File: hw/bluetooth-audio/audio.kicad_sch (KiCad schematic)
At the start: 39 parts, among them J1 AudioJack4_Ground, U4 ES8388

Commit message: Schematic: split supply into separate audio and system 3V3 rails
First design work since the April 2025 production release. Sixteen months of
edits had accumulated uncommitted; this captures the schematic and board state.

Power topology change: the single 3.3 V supply is now two independent rails,
+3V3_SYS and +3V3_AUDIO, each with its own regulator (U7, U8) and test point
(TEST_3V3_SYS, TEST_3V3_AUDIO). This isolates the ES8388 and the mic from the
~250 mA Bluetooth TX bursts on the ESP32 rail, which design-review-v1 flagged
as an S2 defect and the ES8388 user guide asks for directly.

Also addresses the S1 defects from the review (owner-applied): ES8388 CE pin
pulled down to DGND so the I2C address is determined rather than floating, and
the ESP32 CAP1 10 nF cap fitted.

Both rails are currently NCP1117-3.3 in SOT-223. The topology is right but the
parts are not yet the ones specified in docs/requirements-design.md: Rail A
should become AP7361C-33Y5 (SOT-89-5, ultra-low dropout, needed so the rail
survives on battery) and Rail B an LP5907MFX-3.3 (6.5 uVRMS, the point of
having a separate analog rail at all). Two SOT-223 parts also spend board area
the review specifically asked to reclaim.

Co-Authored-By: Claude Opus 5 <noreply@anthropic.com>
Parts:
- added C46: 100nF, Capacitor_SMD:C_0402_1005Metric, symbol Device:C_Small
- added R16: 10R, Resistor_SMD:R_0402_1005Metric, symbol Device:R_Small
- added R27: 10k, Resistor_SMD:R_0402_1005Metric, symbol Device:R_Small
- added U3: TS5A23159DGS, Package_SO:TSSOP-10_3x3mm_P0.5mm, symbol Analog_Switch:TS5A23159DGS
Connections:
- net GND: now also C46.2, R27.2, U3.3 (GND)
- net I2C_AD: no longer U4.26 (CE)
- net LIN2: now also U3.2
- net LOUT1: now also U4.12 (LOUT1), U3.9; no longer J1.T, R7.2
- net RIN2: now also U3.4
- net ROUT1: now also U4.11 (ROUT1), U3.7; no longer J1.R1, R8.2
- net at C25.2: now also U3.6; no longer U4.11 (ROUT1)
- net at C23.2: now also U3.10; no longer U4.12 (LOUT1)
- net +1V8 renamed +3V3_AUDIO
- net +3V3_AUDIO: now also R16.1
- net +3V3 renamed AVDD
- net AVDD: now also C46.1, R16.2, U3.8 (VCC)
- new net: J1.R1, R7.2
- new net: J1.T, R8.2
- new net: R27.1, U4.26 (CE)
- new net AUDIO_IN_EN: U3.5
- new net AUDIO_OUT_EN: U3.1
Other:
- note added: "Separation between digital and audio VCC TODO confirm from Datasheet"
- note added: "TODO replace with 3 pole"
- note removed: "Check connections on audio jack"
- moved on the sheet: J1, TP6

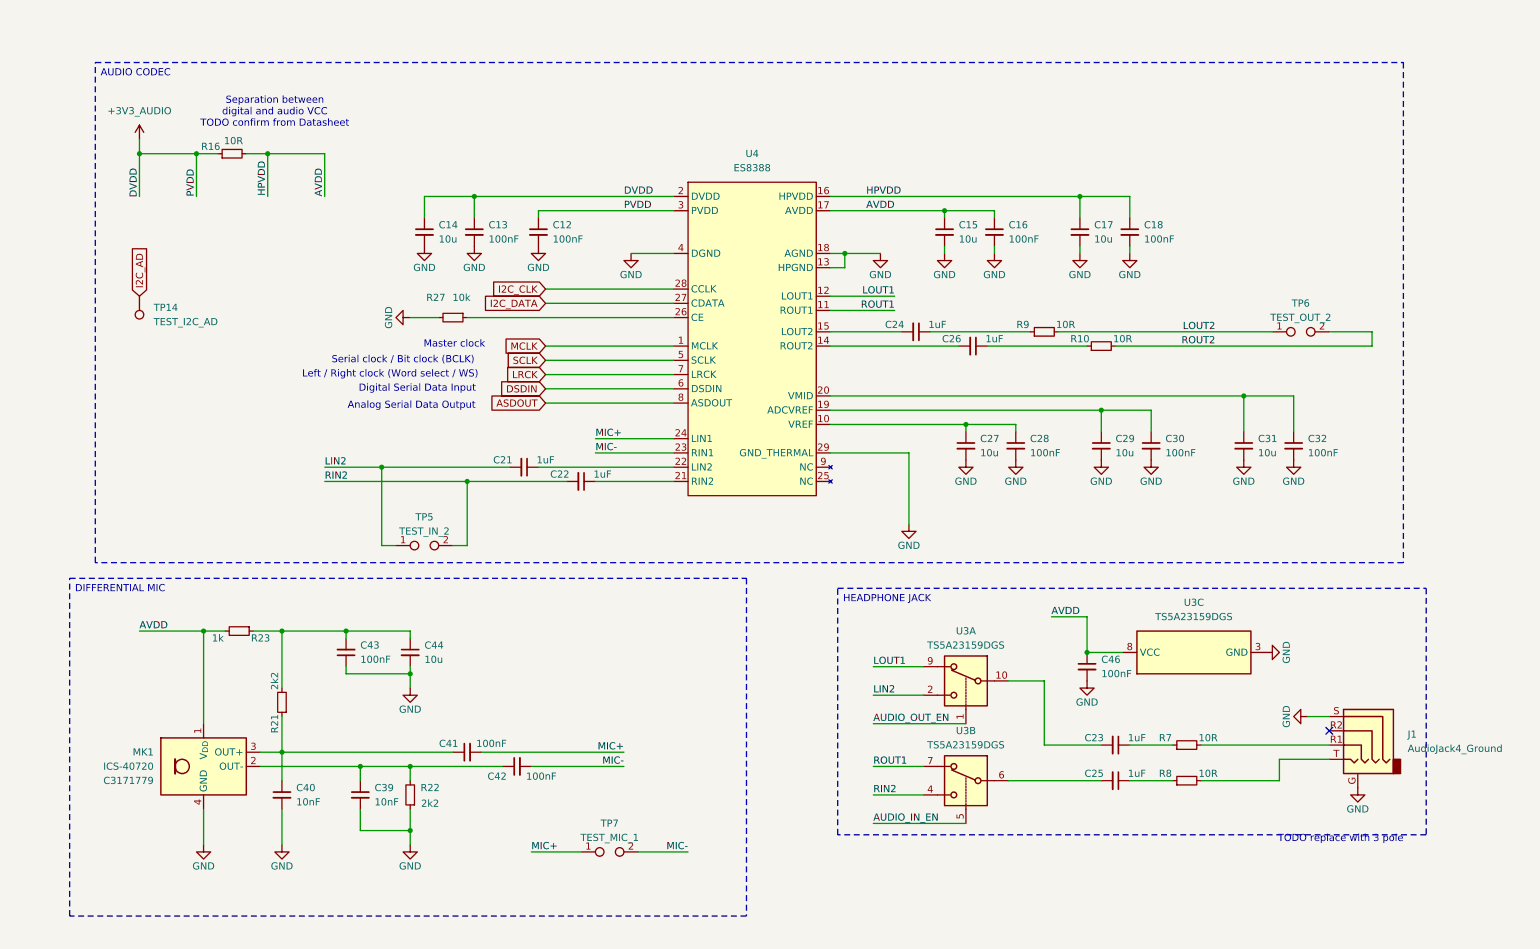
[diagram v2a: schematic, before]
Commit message: Rev B micro sheet: correctness fixes, CH340 load switch, full ESP32 GPIO map
Micro-sheet fixes (netlist-verified):
- UART TX/RX crossover corrected (U0RXD<->CH340 TXD, U0TXD<->CH340 RXD)
- Flash IO2/IO3 uncrossed (GPIO9/SPIWP->IO2, GPIO10/SPIHD->IO3)
- Digital rail unified to +3V3_SYS; EN pull-up (R11) reconnected

CH340K high-side load switch (delta #16):
- Q2 AO3401A (SOT-23, LCSC C15127) + R40 100k gate pull-down = default-ON
  so the ROM bootloader is powered for USB flashing; gate CH340_EN on GPIO21,
  firmware drives high to disable the bridge on battery

Full ESP32 interface wired (see design-overview.md 3.8):
- EN1->16, EN2->17, AUDIO_VCC_EN->4, AUDIO_SW->5, CH340_EN->21, CHARGE_EN->2
- /PGOOD->38, /CHG->32; ADC1 senses BAT_ADC->34, USB_CC1->36, USB_CC2->37,
  USB_VBUS_SENSE->39; GPIO33 spare
- AUDIO_SW drives both TS5A23159 inputs (LOW=RX, HIGH=TX); pinout verified
  against TI datasheet (COM=jack, NC=codec-out, NO=codec-in, both channels)

Docs:
- design-overview.md: committed GPIO map with strapping-pin FW/HW implications
  (3.8), AUDIO_SW/CHARGE_EN firmware notes (9), updated status (10)
- design-review-micro.md: micro-sheet systems review
- added WCH CH340 datasheet; updated TODO
- gitignore MCP snapshot/log artifacts

Co-Authored-By: Claude Opus 4.8 <noreply@anthropic.com>
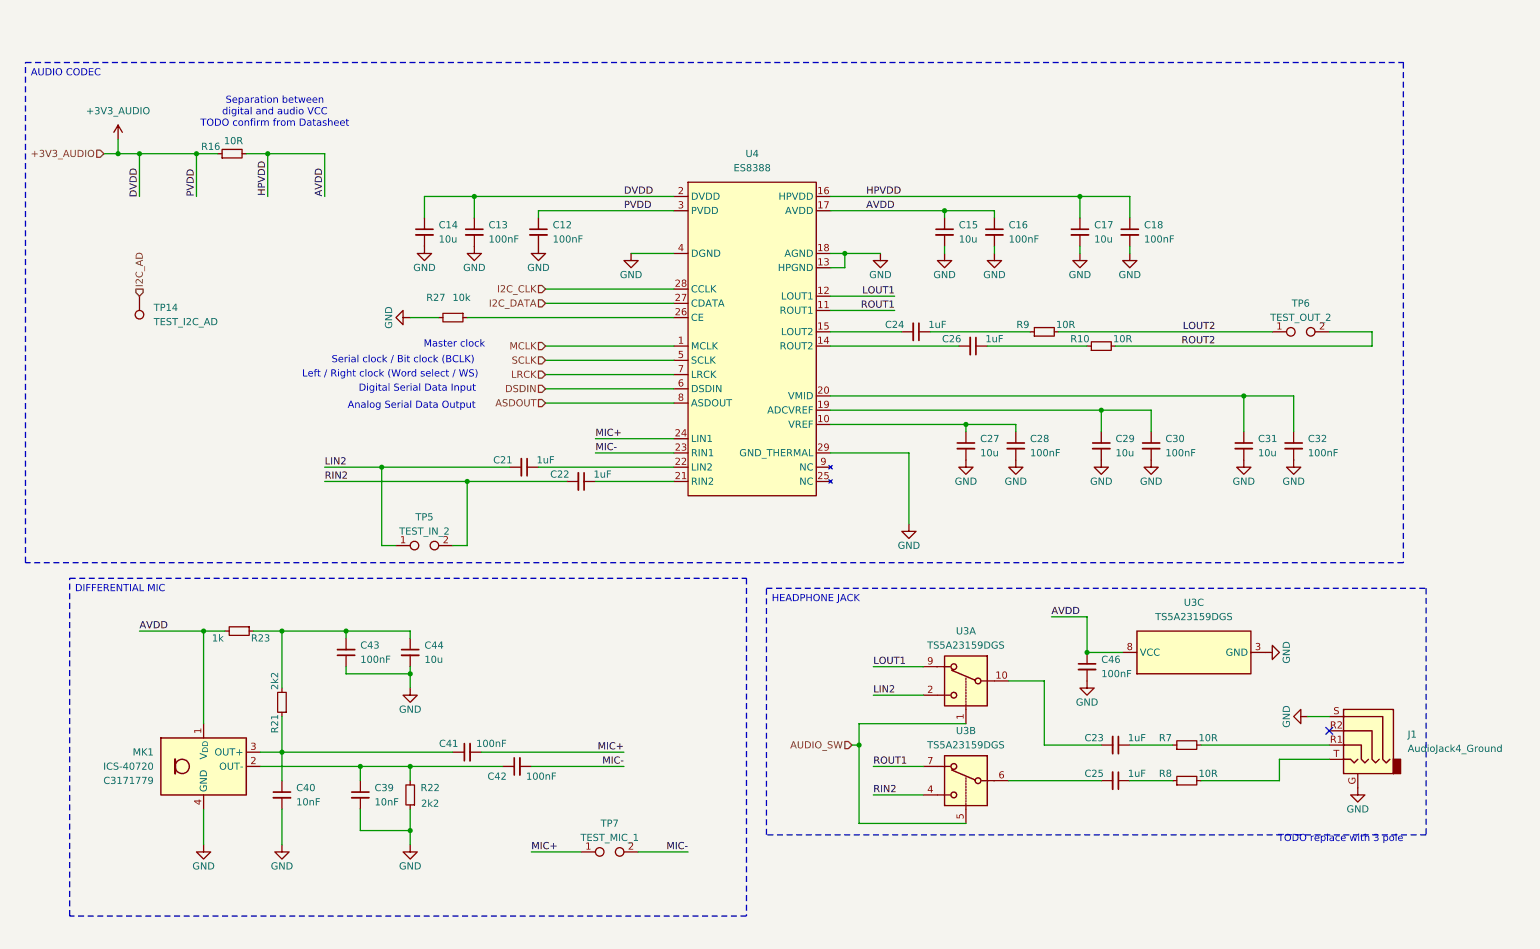
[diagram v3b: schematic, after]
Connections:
- net AUDIO_OUT_EN is gone; now on net AUDIO_SW: U3.1
- net AUDIO_IN_EN renamed AUDIO_SW
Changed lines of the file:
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@@
 	(text_box "HEADPHONE JACK\n"
 		(exclude_from_sim no)
-		(at 165.1 119.38 0)
-		(size 104.902 43.942)
+		(at 152.4 119.38 0)
+		(size 117.602 43.942)
 		(margins 0.9525 0.9525 0.9525 0.9525)
 		(stroke
@@
 	(text_box "AUDIO CODEC\n"
 		(exclude_from_sim no)
-		(at 32.766 25.654 0)
-		(size 233.172 89.154)
+		(at 20.32 25.654 0)
+		(size 245.618 89.154)
 		(margins 0.9525 0.9525 0.9525 0.9525)
 		(stroke
@@
 	)
 	(junction
+		(at 36.83 41.91)
+		(diameter 0)
+		(color 0 0 0 0)
+	)
+	(junction
 		(at 52.07 127)
 		(diameter 0)
@@
 	)
 	(junction
+		(at 168.91 147.32)
+		(diameter 0)
+		(color 0 0 0 0)
+	)
+	(junction
 		(at 88.9 151.13)
 		(diameter 0)
@@
 	(wire
 		(pts
+			(xy 168.91 161.29) (xy 187.96 161.29)
+		)
+		(stroke
+			(width 0)
+			(type default)
+		)
+	)
+	(wire
+		(pts
 			(xy 121.92 100.33) (xy 135.89 100.33)
 		)
@@
 	(wire
 		(pts
+			(xy 34.29 41.91) (xy 36.83 41.91)
+		)
+		(stroke
+			(width 0)
+			(type default)
+		)
+	)
+	(wire
+		(pts
 			(xy 63.5 41.91) (xy 63.5 49.53)
 		)
@@
 	(wire
 		(pts
-			(xy 171.45 143.51) (xy 187.96 143.51)
+			(xy 163.83 67.31) (xy 175.26 67.31)
 		)
 		(stroke
@@
 	(wire
 		(pts
-			(xy 163.83 67.31) (xy 175.26 67.31)
+			(xy 171.45 138.43) (xy 180.34 138.43)
 		)
 		(stroke
@@
 	(wire
 		(pts
-			(xy 171.45 138.43) (xy 180.34 138.43)
+			(xy 113.03 86.36) (xy 135.89 86.36)
 		)
 		(stroke
@@
 	(wire
 		(pts
-			(xy 113.03 86.36) (xy 135.89 86.36)
+			(xy 163.83 49.53) (xy 208.28 49.53)
 		)
 		(stroke
@@
 	(wire
 		(pts
-			(xy 163.83 49.53) (xy 208.28 49.53)
+			(xy 99.06 111.76) (xy 96.52 111.76)
 		)
 		(stroke
@@
 	(wire
 		(pts
-			(xy 99.06 111.76) (xy 96.52 111.76)
+			(xy 36.83 41.91) (xy 40.64 41.91)
 		)
 		(stroke
@@
 	(wire
 		(pts
+			(xy 168.91 147.32) (xy 168.91 161.29)
+		)
+		(stroke
+			(width 0)
+			(type default)
+		)
+	)
+	(wire
+		(pts
 			(xy 80.01 151.13) (xy 88.9 151.13)
 		)
@@
 	(wire
 		(pts
-			(xy 40.64 41.91) (xy 40.64 39.37)
+			(xy 36.83 41.91) (xy 36.83 39.37)
 		)
 		(stroke
@@
 	(wire
 		(pts
+			(xy 168.91 143.51) (xy 187.96 143.51)
+		)
+		(stroke
+			(width 0)
+			(type default)
+		)
+	)
+	(wire
+		(pts
 			(xy 184.15 59.69) (xy 184.15 58.42)
 		)
@@
 	(wire
 		(pts
+			(xy 167.64 147.32) (xy 168.91 147.32)
+		)
+		(stroke
+			(width 0)
+			(type default)
+		)
+	)
+	(wire
+		(pts
 			(xy 209.55 130.81) (xy 215.9 130.81)
 		)
@@
 	(wire
 		(pts
+			(xy 168.91 143.51) (xy 168.91 147.32)
+		)
+		(stroke
+			(width 0)
+			(type default)
+		)
+	)
+	(wire
+		(pts
 			(xy 214.63 76.2) (xy 260.35 76.2)
 		)
@@
 	(wire
 		(pts
-			(xy 171.45 161.29) (xy 187.96 161.29)
-		)
-		(stroke
-			(width 0)
-			(type default)
-		)
-	)
-	(wire
-		(pts
 			(xy 52.07 165.1) (xy 52.07 158.75)
 		)
@@
 		)
 	)
-	(label "AUDIO_IN_EN"
-		(at 171.45 161.29 0)
-		(effects
-			(font
-				(size 1.27 1.27)
-			)
-			(justify left bottom)
-		)
-	)
 	(label "PVDD"
 		(at 50.8 49.53 90)
@@
 		)
 	)
-	(label "AUDIO_OUT_EN"
-		(at 171.45 143.51 0)
-		(effects
-			(font
-				(size 1.27 1.27)
-			)
-			(justify left bottom)
-		)
-	)
 	(label "HPVDD"
 		(at 170.18 49.53 0)
@@
 		)
 	)
-	(global_label "LRCK"
+	(hierarchical_label "LRCK"
 		(shape input)
 		(at 113.03 81.28 180)
-		(fields_autoplaced yes)
 		(effects
 			(font
@@
 			(justify right)
 		)
-		(property "Intersheetrefs" "${INTERSHEET_REFS}"
-			(at 105.2067 81.28 0)
-			(hide yes)
-			(show_name no)
-			(do_not_autoplace no)
-			(effects
-				(font
-					(size 1.27 1.27)
-				)
-				(justify right)
+	)
+	(hierarchical_label "I2C_AD"
+		(shape input)
+		(at 40.64 67.31 90)
+		(effects
+			(font
+				(size 1.27 1.27)
 			)
+			(justify left)
 		)
 	)
-	(global_label "I2C_DATA"
+	(hierarchical_label "I2C_CLK"
 		(shape input)
-		(at 113.03 68.58 180)
-		(fields_autoplaced yes)
+		(at 113.03 66.04 180)
 		(effects
 			(font
@@
 			(justify right)
 		)
-		(property "Intersheetrefs" "${INTERSHEET_REFS}"
-			(at 101.5781 68.58 0)
-			(hide yes)
-			(show_name no)
-			(do_not_autoplace no)
-			(effects
-				(font
-					(size 1.27 1.27)
-				)
-				(justify right)
+	)
+	(hierarchical_label "+3V3_AUDIO"
+		(shape input)
+		(at 34.29 41.91 180)
+		(effects
+			(font
+				(size 1.27 1.27)
 			)
+			(justify right)
 		)
 	)
-	(global_label "DSDIN"
+	(hierarchical_label "DSDIN"
 		(shape input)
 		(at 113.03 83.82 180)
-		(fields_autoplaced yes)
 		(effects
 			(font
@@
 			(justify right)
 		)
-		(property "Intersheetrefs" "${INTERSHEET_REFS}"
-			(at 104.36 83.82 0)
-			(hide yes)
-			(show_name no)
-			(do_not_autoplace no)
-			(effects
-				(font
-					(size 1.27 1.27)
-				)
-				(justify right)
-			)
-		)
 	)
-	(global_label "I2C_CLK"
+	(hierarchical_label "I2C_DATA"
 		(shape input)
-		(at 113.03 66.04 180)
-		(fields_autoplaced yes)
+		(at 113.03 68.58 180)
 		(effects
 			(font
@@
 			(justify right)
 		)
-		(property "Intersheetrefs" "${INTERSHEET_REFS}"
-			(at 102.4248 66.04 0)
-			(hide yes)
-			(show_name no)
-			(do_not_autoplace no)
-			(effects
-				(font
-					(size 1.27 1.27)
-				)
-				(justify right)
-			)
-		)
 	)
-	(global_label "SCLK"
+	(hierarchical_label "MCLK"
 		(shape input)
-		(at 113.03 78.74 180)
-		(fields_autoplaced yes)
+		(at 113.03 76.2 180)
 		(effects
 			(font
@@
 			(justify right)
 		)
-		(property "Intersheetrefs" "${INTERSHEET_REFS}"
-			(at 105.2672 78.74 0)
-			(hide yes)
-			(show_name no)
-			(do_not_autoplace no)
-			(effects
-				(font
-					(size 1.27 1.27)
-				)
-				(justify right)
-			)
-		)
 	)
-	(global_label "I2C_AD"
+	(hierarchical_label "AUDIO_SW"
 		(shape input)
-		(at 40.64 67.31 90)
-		(fields_autoplaced yes)
+		(at 167.64 147.32 180)
 		(effects
 			(font
 				(size 1.27 1.27)
 			)
-			(justify left)
-		)
-		(property "Intersheetrefs" "${INTERSHEET_REFS}"
-			(at 40.64 57.9143 90)
-			(hide yes)
-			(show_name no)
-			(do_not_autoplace no)
-			(effects
-				(font
-					(size 1.27 1.27)
-				)
-				(justify left)
-			)
+			(justify right)
 		)
 	)
-	(global_label "MCLK"
+	(hierarchical_label "SCLK"
 		(shape input)
-		(at 113.03 76.2 180)
-		(fields_autoplaced yes)
+		(at 113.03 78.74 180)
 		(effects
 			(font
@@
 			(justify right)
 		)
-		(property "Intersheetrefs" "${INTERSHEET_REFS}"
-			(at 105.0253 76.2 0)
-			(hide yes)
-			(show_name no)
-			(do_not_autoplace no)
-			(effects
-				(font
-					(size 1.27 1.27)
-				)
-				(justify right)
-			)
-		)
 	)
-	(global_label "ASDOUT"
+	(hierarchical_label "ASDOUT"
 		(shape input)
 		(at 113.03 86.36 180)
-		(fields_autoplaced yes)
 		(effects
 			(font
@@
 			(justify right)
 		)
-		(property "Intersheetrefs" "${INTERSHEET_REFS}"
-			(at 102.8481 86.36 0)
-			(hide yes)
-			(show_name no)
-			(do_not_autoplace no)
-			(effects
-				(font
-					(size 1.27 1.27)
-				)
-				(justify right)
-			)
-		)
 	)
 	(symbol
@@
 	(symbol
 		(lib_id "power:+3V3")
-		(at 40.64 39.37 0)
+		(at 36.83 39.37 0)
 		(unit 1)
 		(body_style 1)
@@
 		(fields_autoplaced yes)
 		(property "Reference" "#PWR058"
-			(at 40.64 43.18 0)
+			(at 36.83 43.18 0)
 			(hide yes)
 			(show_name no)
@@
 		)
 		(property "Value" "+3V3_AUDIO"
-			(at 40.64 34.29 0)
+			(at 36.83 34.29 0)
 			(show_name no)
 			(do_not_autoplace no)
@@
 		)
 		(property "Footprint" ""
-			(at 40.64 39.37 0)
+			(at 36.83 39.37 0)
 			(hide yes)
 			(show_name no)
@@
 		)
 		(property "Datasheet" ""
-			(at 40.64 39.37 0)
+			(at 36.83 39.37 0)
 			(hide yes)
 			(show_name no)
@@
 		)
 		(property "Description" ""
-			(at 40.64 39.37 0)
+			(at 36.83 39.37 0)
 			(hide yes)
 			(show_name no)

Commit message: Audio sheet redesign: ZTS6216 mic, PJ-3537S jack, shared 47 uF coupling
Rework the audio subsystem and record the rationale.

- Microphone: switch to ZillTek ZTS6216 (self-biased single-ended, C0G
  mic coupling C41/C42 per datasheet); pseudo-diff RIN1 provisioned DNP.
- Jack: PJ-3537S 3-pole TRS + detect switch (custom symbol + footprint).
- Coupling: single shared 47 uF electrolytic pair (C1/C21) on the jack
  side of the TX/RX switch, serving both RX and TX; R22/R23 bleed.
- TX input: BAT54S series-Schottky clamps (D7/D8) to AVDD/GND,
  line-level-only, PGA 0 dB.
- Ground loop: battery-only playback is the plan of record (no
  transformer footprint).
- Add TS5A23159 switch, ZTS6216 and PJ-3537S datasheets.
- Add systems design review (docs/design-review-audio.md) and update
  design overview with coupling-cap sizing.
- PCB layout updated to match.

Co-Authored-By: Claude Opus 4.8 <noreply@anthropic.com>
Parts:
- removed C21, C22, C23, C25: 1uF, Capacitor_SMD:C_0402_1005Metric, symbol Device:C_Small
- removed C39, C40: 10nF, Capacitor_SMD:C_0402_1005Metric, symbol Device:C_Small
- removed J1: AudioJack4_Ground, Connector_Audio:Jack_3.5mm_KoreanHropartsElec_PJ-320D-4A_Horizontal, symbol Connector_Audio:AudioJack4_Ground
- removed MK1: ICS-40720, custom_footprints:ICS40720, symbol custom_symbols:ICS-40720
- removed TP7: TEST_MIC_1, custom_footprints:TestPoint_Pad_2x1_D1.0mm, symbol Connector:TestPoint_2Pole
- added C1, C21: 47uF, Capacitor_SMD:CP_Elec_5x5.8, symbol Device:C_Polarized_US
- added C54: 100nF, Capacitor_SMD:C_1206_3216Metric_Pad1.33x1.80mm_HandSolder, symbol Device:C_Small
- added D7, D8: D_Schottky_Dual_Series_AKC_Split, Package_TO_SOT_SMD:SOT-23, symbol Device:D_Schottky_Dual_Series_AKC_Split
- added J1: PJ-3537S-SMT, custom_footprints:PJ-3537S-SMT, symbol custom_symbols:PJ-3537S-SMT
- added MK1: ZTS6216, custom_footprints:ZTS6216, symbol custom_symbols:ZTS6216
- added R19, R20: 1k, Resistor_SMD:R_0402_1005Metric, symbol Device:R_Small
- added R41: 0R, Resistor_SMD:R_0402_1005Metric, symbol Device:R_Small
- C41, C42: footprint Capacitor_SMD:C_0402_1005Metric -> Capacitor_SMD:C_1206_3216Metric_Pad1.33x1.80mm_HandSolder; Supplier Part Number (none) -> C97946
- R21: value 2k2 -> 10R
- R22: value 2k2 -> 100k
- R23: value 1k -> 100k
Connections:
- net +3V3_AUDIO: now also R21.1, R19.2, R20.2
- net AVDD: now also C43.2, C44.1, R21.2, D7.2 (K), D8.2 (K), MK1.4 (VDD); no longer C17.1, C18.1, R16.2, R23.2, U4.16 (HPVDD)
- net GND: now also C42.1, R23.1, C54.1, D7.1 (A), D8.1 (A), J1.1 (SLEEVE), J1.2 (GND), MK1.2 (GND), MK1.3 (GND)
- net I2C_CLK: now also R19.1
- net I2C_DATA: now also R20.1
- net LIN2: now also U3.4, U4.22 (LIN2), D8.3 (K), D8.3 (K); no longer U3.2
- net LOUT1: now also U3.7; no longer U3.9
- net RIN2: now also U3.2, U4.21 (RIN2), D7.3 (K), D7.3 (K); no longer U3.4
- net ROUT1: now also U3.9; no longer U3.7
- net at C41.1: now also MK1.1 (OUT); no longer R21.1
- net at R7.2: now also J1.3 (RING_RIGHT)
- net at R8.2: now also J1.4 (TIP_LEFT)
- net at U3.6: now also C21.1
- net at R22.2: now also R8.1, C21.2; no longer C42.1
- net at R7.1: now also R23.2, C1.2
- net at U3.10: now also C1.1
- net MIC+ renamed MIC_P
- net MIC- renamed MIC_N
- net MIC_N: now also R41.1; no longer U4.23 (RIN1)
- new net HPVDD: C17.1, C18.1, R16.2, U4.16 (HPVDD)
- new net MIC_N_UC: C54.2, R41.2, U4.23 (RIN1)
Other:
- note added: "Anti-thump bleed resistors"
- note added: "Change dielectric"
- note added: "Populate R41 + either C42/C54 to configure pseudo-differential mic"
- note removed: "Separation between digital and audio VCC TODO confirm from Datasheet"
- note removed: "TODO replace with 3 pole"
- moved on the sheet: C12, C13, C14, C41, C43, C44, C46, R7, R8, TP5, U3A, U3B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
